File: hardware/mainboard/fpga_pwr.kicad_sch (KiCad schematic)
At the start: 15 parts

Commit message: Connecting up various bits
Signed-off-by: David Shah <dave@ds0.me>
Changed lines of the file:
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@@
   (symbol (lib_id "meowality:LIFCL_40_CABGA400") (at 67.31 43.18 0) (unit 1)
     (in_bom yes) (on_board yes)
-    (property "Reference" "U?" (id 0) (at 233.0451 148.5062 0)
+    (property "Reference" "U?" (id 0) (at 68.58 41.91 0)
       (effects (font (size 1.524 1.524)) (justify left))
     )

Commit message: More stuff
Signed-off-by: David Shah <dave@ds0.me>
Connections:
- net PCIE_CLK+ renamed NX_REFCLK+
- net PCIE_CLK- renamed NX_REFCLK-
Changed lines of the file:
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@@
     (stroke (width 0) (type solid) (color 0 0 0 0))
   )
-  (global_label "PCIE_CLK+" (shape input) (at 58.42 254 180)
+  (global_label "NX_REFCLK+" (shape input) (at 58.42 254 180)
     (effects (font (size 1.27 1.27)) (justify right))
-    (property "Intersheet References" "${INTERSHEET_REFS}" (id 0) (at 44.081 253.9206 0)
+    (property "Intersheet References" "${INTERSHEET_REFS}" (id 0) (at 42.3272 254.0794 0)
       (effects (font (size 1.27 1.27)) (justify right) hide)
     )
   )
-  (global_label "PCIE_CLK-" (shape input) (at 58.42 256.54 180)
+  (global_label "NX_REFCLK-" (shape input) (at 58.42 256.54 180)
     (effects (font (size 1.27 1.27)) (justify right))
-    (property "Intersheet References" "${INTERSHEET_REFS}" (id 0) (at 44.081 256.4606 0)
+    (property "Intersheet References" "${INTERSHEET_REFS}" (id 0) (at 42.3272 256.6194 0)
       (effects (font (size 1.27 1.27)) (justify right) hide)
     )

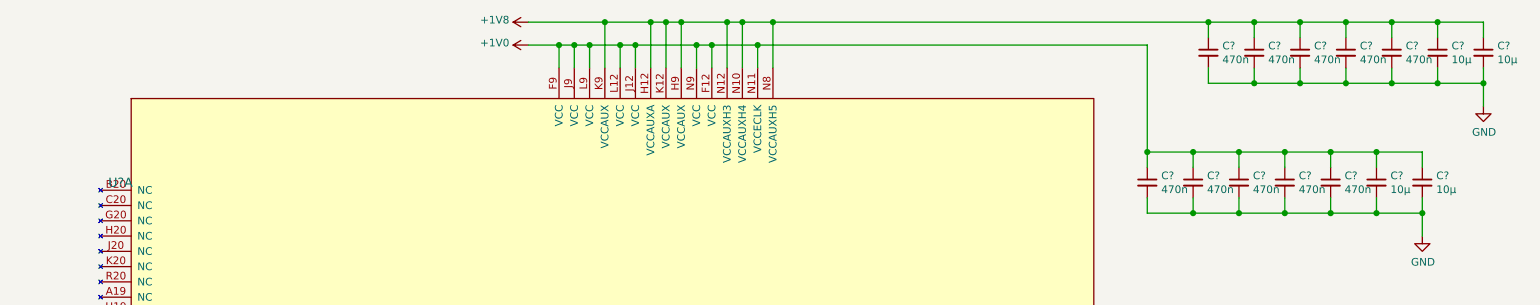
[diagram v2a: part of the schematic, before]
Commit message: Annotate and assign some footpints
Signed-off-by: David Shah <dave@ds0.me>
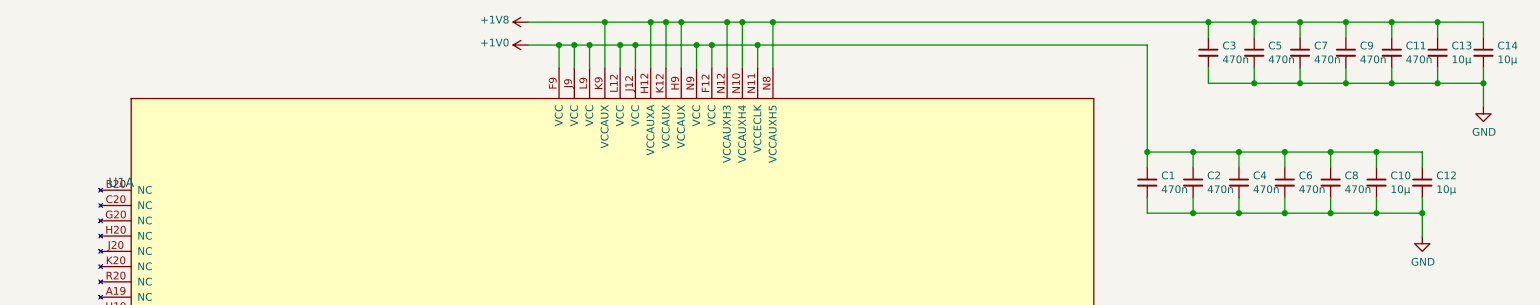
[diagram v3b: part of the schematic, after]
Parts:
- C1, C11, C2, C3, C4, C5, C6, C7, C8, C9: renamed from C?; footprint (none) -> Capacitor_SMD:C_0402_1005Metric
- C10, C12, C13, C14: renamed from C?; footprint (none) -> Capacitor_SMD:C_0805_2012Metric
- gave numbers to parts that had none: 1
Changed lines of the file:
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@@
   (symbol (lib_id "power:+1V8") (at 138.43 15.24 90) (unit 1)
     (in_bom yes) (on_board yes)
-    (property "Reference" "#PWR?" (id 0) (at 142.24 15.24 0)
+    (property "Reference" "#PWR02" (id 0) (at 142.24 15.24 0)
       (effects (font (size 1.27 1.27)) hide)
     )
@@
   (symbol (lib_id "power:+1V0") (at 138.43 19.05 90) (unit 1)
     (in_bom yes) (on_board yes)
-    (property "Reference" "#PWR?" (id 0) (at 142.24 19.05 0)
+    (property "Reference" "#PWR03" (id 0) (at 142.24 19.05 0)
       (effects (font (size 1.27 1.27)) hide)
     )
@@
   (symbol (lib_id "power:GND") (at 85.09 279.4 270) (unit 1)
     (in_bom yes) (on_board yes)
-    (property "Reference" "#PWR?" (id 0) (at 78.74 279.4 0)
+    (property "Reference" "#PWR01" (id 0) (at 78.74 279.4 0)
       (effects (font (size 1.27 1.27)) hide)
     )
@@
   (symbol (lib_id "power:GND") (at 287.02 50.8 0) (unit 1)
     (in_bom yes) (on_board yes)
-    (property "Reference" "#PWR?" (id 0) (at 287.02 57.15 0)
+    (property "Reference" "#PWR04" (id 0) (at 287.02 57.15 0)
       (effects (font (size 1.27 1.27)) hide)
     )
@@
   (symbol (lib_id "power:GND") (at 297.18 29.21 0) (unit 1)
     (in_bom yes) (on_board yes)
-    (property "Reference" "#PWR?" (id 0) (at 297.18 35.56 0)
+    (property "Reference" "#PWR05" (id 0) (at 297.18 35.56 0)
       (effects (font (size 1.27 1.27)) hide)
     )
@@
   (symbol (lib_id "Device:C_Small") (at 241.3 41.91 0) (unit 1)
     (in_bom yes) (on_board yes)
-    (property "Reference" "C?" (id 0) (at 243.6242 40.7606 0)
+    (property "Reference" "C1" (id 0) (at 243.6242 40.7606 0)
       (effects (font (size 1.27 1.27)) (justify left))
     )
@@
       (effects (font (size 1.27 1.27)) (justify left))
     )
-    (property "Footprint" "" (id 2) (at 241.3 41.91 0)
+    (property "Footprint" "Capacitor_SMD:C_0402_1005Metric" (id 2) (at 241.3 41.91 0)
       (effects (font (size 1.27 1.27)) hide)
     )
@@
   (symbol (lib_id "Device:C_Small") (at 248.92 41.91 0) (unit 1)
     (in_bom yes) (on_board yes)
-    (property "Reference" "C?" (id 0) (at 251.2442 40.7606 0)
+    (property "Reference" "C2" (id 0) (at 251.2442 40.7606 0)
       (effects (font (size 1.27 1.27)) (justify left))
     )
@@
       (effects (font (size 1.27 1.27)) (justify left))
     )
-    (property "Footprint" "" (id 2) (at 248.92 41.91 0)
+    (property "Footprint" "Capacitor_SMD:C_0402_1005Metric" (id 2) (at 248.92 41.91 0)
       (effects (font (size 1.27 1.27)) hide)
     )
@@
   (symbol (lib_id "Device:C_Small") (at 251.46 20.32 0) (unit 1)
     (in_bom yes) (on_board yes)
-    (property "Reference" "C?" (id 0) (at 253.7842 19.1706 0)
+    (property "Reference" "C3" (id 0) (at 253.7842 19.1706 0)
       (effects (font (size 1.27 1.27)) (justify left))
     )
@@
       (effects (font (size 1.27 1.27)) (justify left))
     )
-    (property "Footprint" "" (id 2) (at 251.46 20.32 0)
+    (property "Footprint" "Capacitor_SMD:C_0402_1005Metric" (id 2) (at 251.46 20.32 0)
       (effects (font (size 1.27 1.27)) hide)
     )
@@
   (symbol (lib_id "Device:C_Small") (at 256.54 41.91 0) (unit 1)
     (in_bom yes) (on_board yes)
-    (property "Reference" "C?" (id 0) (at 258.8642 40.7606 0)
+    (property "Reference" "C4" (id 0) (at 258.8642 40.7606 0)
       (effects (font (size 1.27 1.27)) (justify left))
     )
@@
       (effects (font (size 1.27 1.27)) (justify left))
     )
-    (property "Footprint" "" (id 2) (at 256.54 41.91 0)
+    (property "Footprint" "Capacitor_SMD:C_0402_1005Metric" (id 2) (at 256.54 41.91 0)
       (effects (font (size 1.27 1.27)) hide)
     )
@@
   (symbol (lib_id "Device:C_Small") (at 259.08 20.32 0) (unit 1)
     (in_bom yes) (on_board yes)
-    (property "Reference" "C?" (id 0) (at 261.4042 19.1706 0)
+    (property "Reference" "C5" (id 0) (at 261.4042 19.1706 0)
       (effects (font (size 1.27 1.27)) (justify left))
     )
@@
       (effects (font (size 1.27 1.27)) (justify left))
     )
-    (property "Footprint" "" (id 2) (at 259.08 20.32 0)
+    (property "Footprint" "Capacitor_SMD:C_0402_1005Metric" (id 2) (at 259.08 20.32 0)
       (effects (font (size 1.27 1.27)) hide)
     )
@@
   (symbol (lib_id "Device:C_Small") (at 264.16 41.91 0) (unit 1)
     (in_bom yes) (on_board yes)
-    (property "Reference" "C?" (id 0) (at 266.4842 40.7606 0)
+    (property "Reference" "C6" (id 0) (at 266.4842 40.7606 0)
       (effects (font (size 1.27 1.27)) (justify left))
     )
@@
       (effects (font (size 1.27 1.27)) (justify left))
     )
-    (property "Footprint" "" (id 2) (at 264.16 41.91 0)
+    (property "Footprint" "Capacitor_SMD:C_0402_1005Metric" (id 2) (at 264.16 41.91 0)
       (effects (font (size 1.27 1.27)) hide)
     )
@@
   (symbol (lib_id "Device:C_Small") (at 266.7 20.32 0) (unit 1)
     (in_bom yes) (on_board yes)
-    (property "Reference" "C?" (id 0) (at 269.0242 19.1706 0)
+    (property "Reference" "C7" (id 0) (at 269.0242 19.1706 0)
       (effects (font (size 1.27 1.27)) (justify left))
     )
@@
       (effects (font (size 1.27 1.27)) (justify left))
     )
-    (property "Footprint" "" (id 2) (at 266.7 20.32 0)
+    (property "Footprint" "Capacitor_SMD:C_0402_1005Metric" (id 2) (at 266.7 20.32 0)
       (effects (font (size 1.27 1.27)) hide)
     )
@@
   (symbol (lib_id "Device:C_Small") (at 271.78 41.91 0) (unit 1)
     (in_bom yes) (on_board yes)
-    (property "Reference" "C?" (id 0) (at 274.1042 40.7606 0)
+    (property "Reference" "C8" (id 0) (at 274.1042 40.7606 0)
       (effects (font (size 1.27 1.27)) (justify left))
     )
@@
       (effects (font (size 1.27 1.27)) (justify left))
     )
-    (property "Footprint" "" (id 2) (at 271.78 41.91 0)
+    (property "Footprint" "Capacitor_SMD:C_0402_1005Metric" (id 2) (at 271.78 41.91 0)
       (effects (font (size 1.27 1.27)) hide)
     )
@@
   (symbol (lib_id "Device:C_Small") (at 274.32 20.32 0) (unit 1)
     (in_bom yes) (on_board yes)
-    (property "Reference" "C?" (id 0) (at 276.6442 19.1706 0)
+    (property "Reference" "C9" (id 0) (at 276.6442 19.1706 0)
       (effects (font (size 1.27 1.27)) (justify left))
     )
@@
       (effects (font (size 1.27 1.27)) (justify left))
     )
-    (property "Footprint" "" (id 2) (at 274.32 20.32 0)
+    (property "Footprint" "Capacitor_SMD:C_0402_1005Metric" (id 2) (at 274.32 20.32 0)
       (effects (font (size 1.27 1.27)) hide)
     )
@@
   (symbol (lib_id "Device:C_Small") (at 279.4 41.91 0) (unit 1)
     (in_bom yes) (on_board yes)
-    (property "Reference" "C?" (id 0) (at 281.7242 40.7606 0)
+    (property "Reference" "C10" (id 0) (at 281.7242 40.7606 0)
       (effects (font (size 1.27 1.27)) (justify left))
     )
@@
       (effects (font (size 1.27 1.27)) (justify left))
     )
-    (property "Footprint" "" (id 2) (at 279.4 41.91 0)
+    (property "Footprint" "Capacitor_SMD:C_0805_2012Metric" (id 2) (at 279.4 41.91 0)
       (effects (font (size 1.27 1.27)) hide)
     )
@@
   (symbol (lib_id "Device:C_Small") (at 281.94 20.32 0) (unit 1)
     (in_bom yes) (on_board yes)
-    (property "Reference" "C?" (id 0) (at 284.2642 19.1706 0)
+    (property "Reference" "C11" (id 0) (at 284.2642 19.1706 0)
       (effects (font (size 1.27 1.27)) (justify left))
     )
@@
       (effects (font (size 1.27 1.27)) (justify left))
     )
-    (property "Footprint" "" (id 2) (at 281.94 20.32 0)
+    (property "Footprint" "Capacitor_SMD:C_0402_1005Metric" (id 2) (at 281.94 20.32 0)
       (effects (font (size 1.27 1.27)) hide)
     )
@@
   (symbol (lib_id "Device:C_Small") (at 287.02 41.91 0) (unit 1)
     (in_bom yes) (on_board yes)
-    (property "Reference" "C?" (id 0) (at 289.3442 40.7606 0)
+    (property "Reference" "C12" (id 0) (at 289.3442 40.7606 0)
       (effects (font (size 1.27 1.27)) (justify left))
     )
@@
       (effects (font (size 1.27 1.27)) (justify left))
     )
-    (property "Footprint" "" (id 2) (at 287.02 41.91 0)
+    (property "Footprint" "Capacitor_SMD:C_0805_2012Metric" (id 2) (at 287.02 41.91 0)
       (effects (font (size 1.27 1.27)) hide)
     )
@@
   (symbol (lib_id "Device:C_Small") (at 289.56 20.32 0) (unit 1)
     (in_bom yes) (on_board yes)
-    (property "Reference" "C?" (id 0) (at 291.8842 19.1706 0)
+    (property "Reference" "C13" (id 0) (at 291.8842 19.1706 0)
       (effects (font (size 1.27 1.27)) (justify left))
     )
@@
       (effects (font (size 1.27 1.27)) (justify left))
     )
-    (property "Footprint" "" (id 2) (at 289.56 20.32 0)
+    (property "Footprint" "Capacitor_SMD:C_0805_2012Metric" (id 2) (at 289.56 20.32 0)
       (effects (font (size 1.27 1.27)) hide)
     )
@@
   (symbol (lib_id "Device:C_Small") (at 297.18 20.32 0) (unit 1)
     (in_bom yes) (on_board yes)
-    (property "Reference" "C?" (id 0) (at 299.5042 19.1706 0)
+    (property "Reference" "C14" (id 0) (at 299.5042 19.1706 0)
       (effects (font (size 1.27 1.27)) (justify left))
     )
@@
       (effects (font (size 1.27 1.27)) (justify left))
     )
-    (property "Footprint" "" (id 2) (at 297.18 20.32 0)
+    (property "Footprint" "Capacitor_SMD:C_0805_2012Metric" (id 2) (at 297.18 20.32 0)
       (effects (font (size 1.27 1.27)) hide)
     )
@@
   (symbol (lib_id "meowality:LIFCL_40_CABGA400") (at 67.31 43.18 0) (unit 1)
     (in_bom yes) (on_board yes)
-    (property "Reference" "U?" (id 0) (at 68.58 41.91 0)
+    (property "Reference" "U1" (id 0) (at 68.58 41.91 0)
       (effects (font (size 1.524 1.524)) (justify left))
     )

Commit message: Add and assign more footprints
Signed-off-by: David Shah <dave@ds0.me>
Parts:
- U1: footprint (none) -> meowality:BGA-400_20x20_17.0x17.0mm
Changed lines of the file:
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@@
       (effects (font (size 1.524 1.524)) (justify left))
     )
-    (property "Footprint" "" (id 2) (at 71.12 41.91 0)
+    (property "Footprint" "meowality:BGA-400_20x20_17.0x17.0mm" (id 2) (at 71.12 41.91 0)
       (effects (font (size 1.524 1.524)) (justify right) hide)
     )
